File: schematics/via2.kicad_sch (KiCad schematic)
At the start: 12 parts, among them J11 Port A, J12 Port B, J13 myBus, Q2 2SB817, U10 W65C22, U11 74HC238

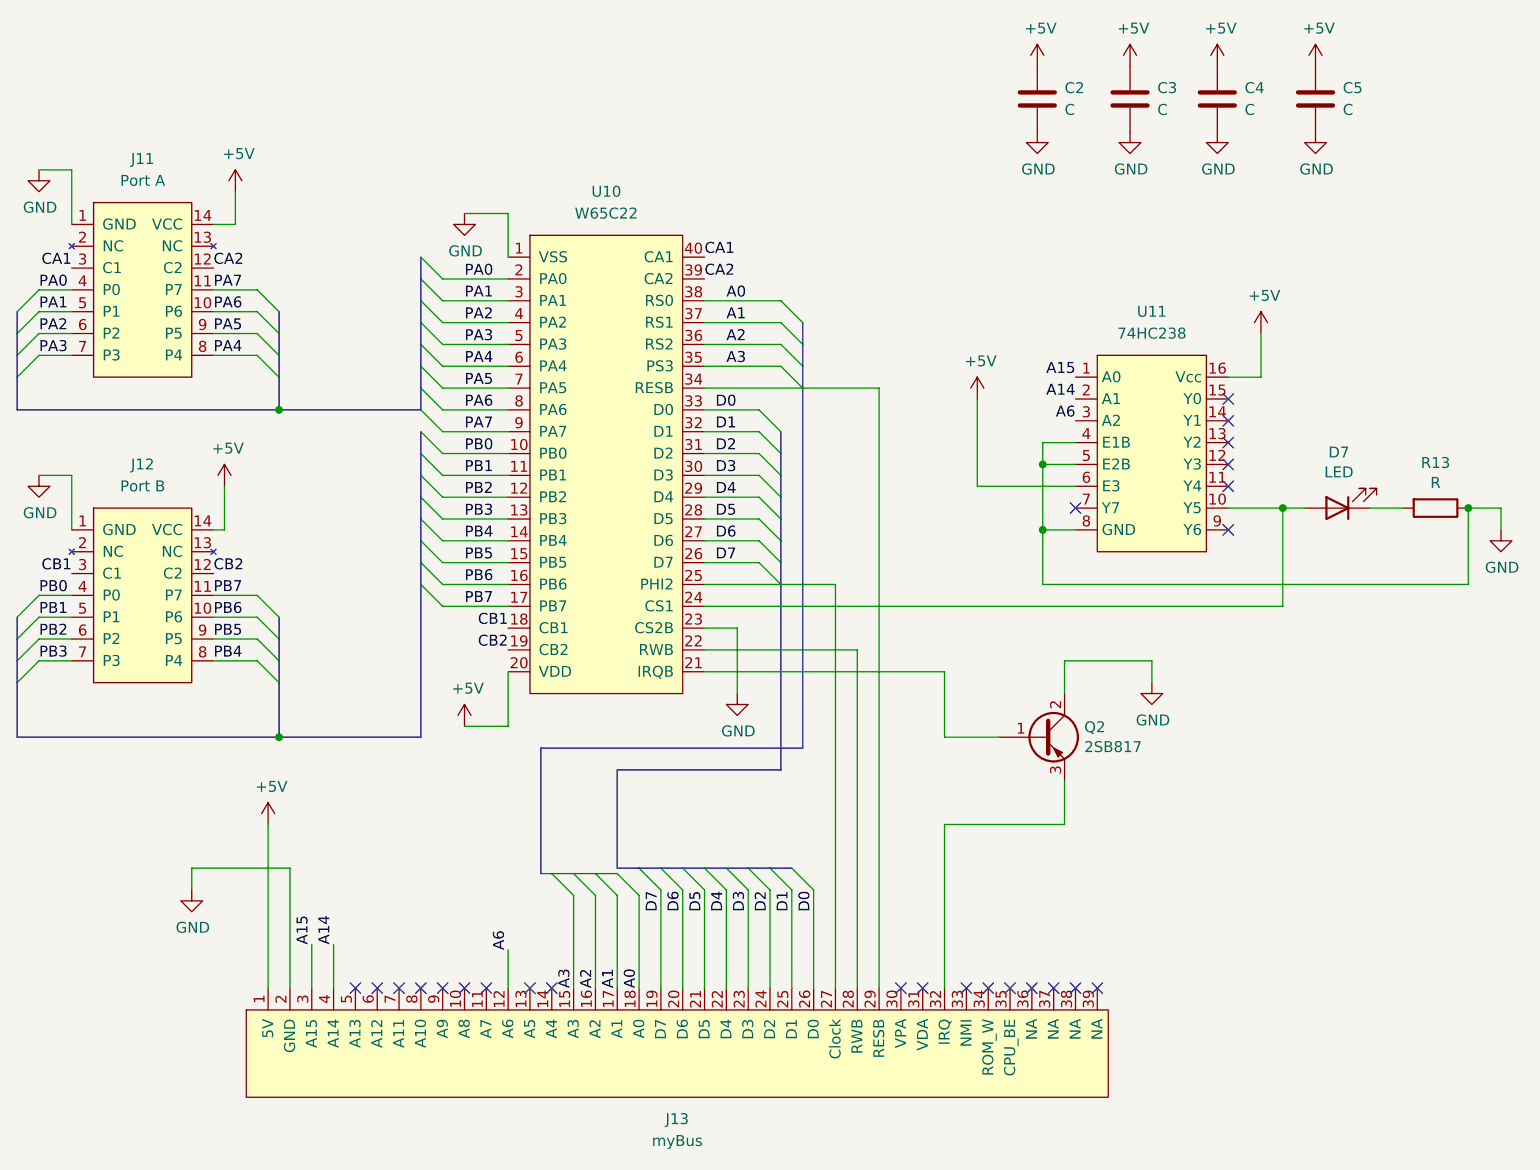
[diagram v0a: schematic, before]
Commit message: Fix errors in schematics
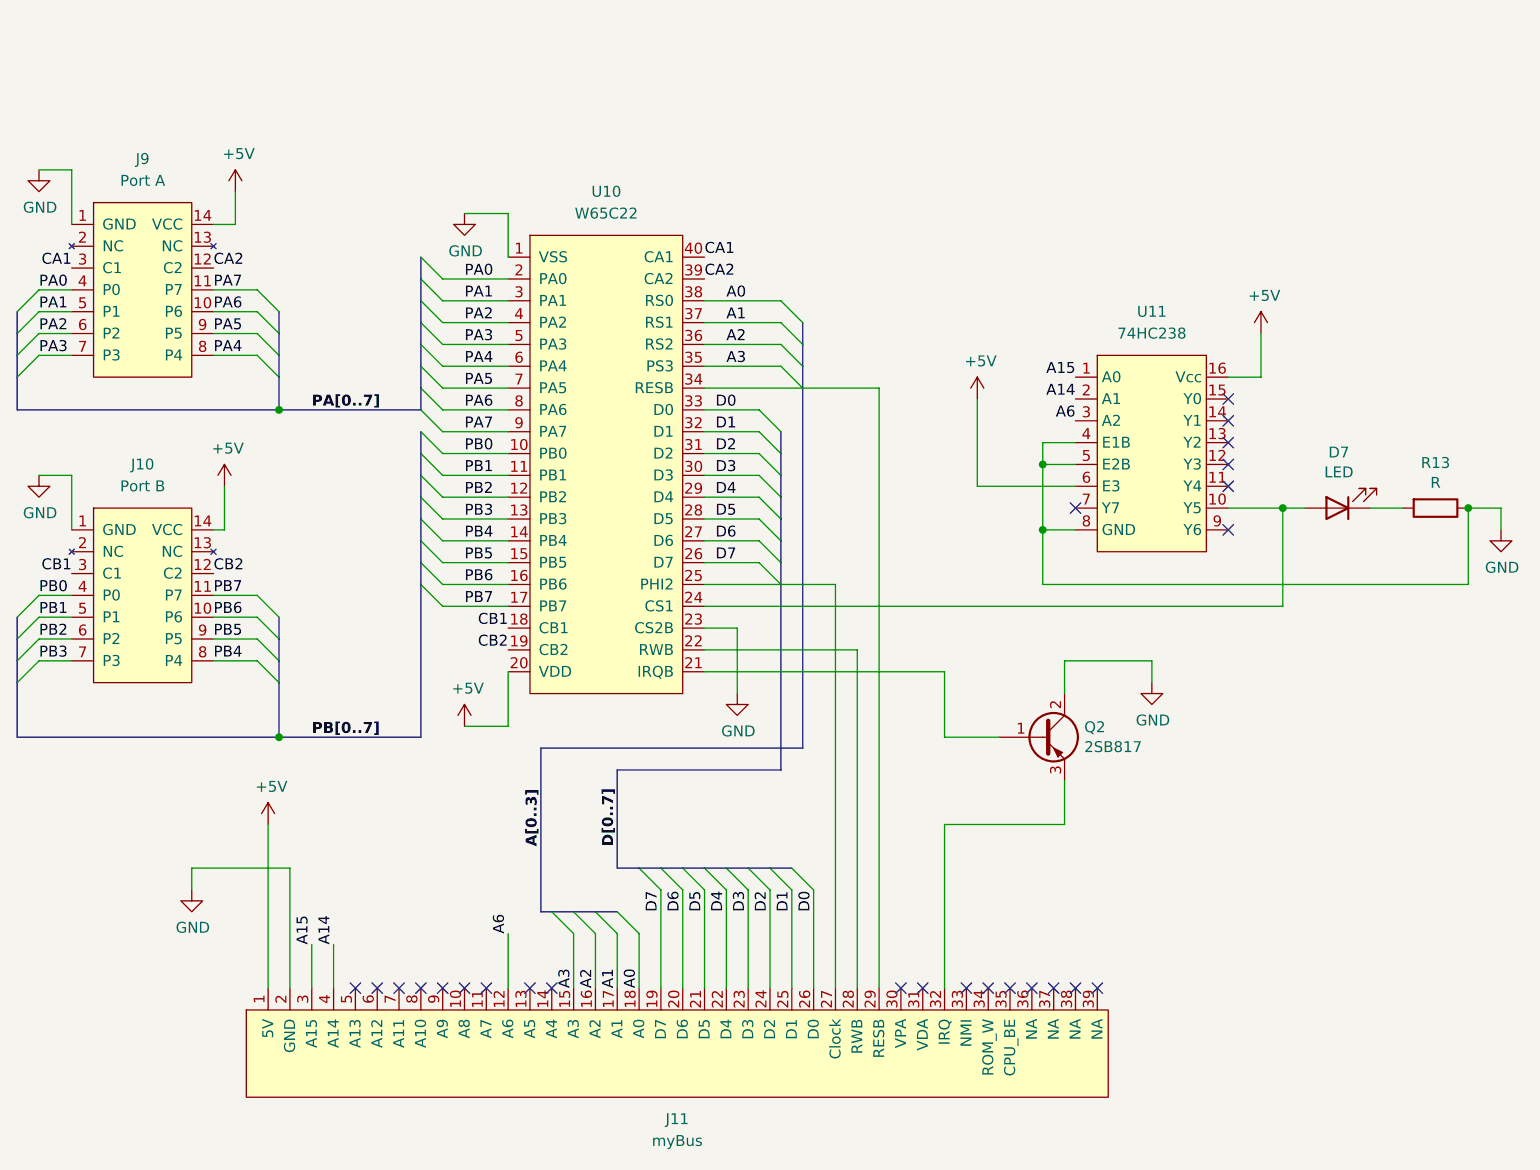
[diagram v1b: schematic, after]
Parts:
- removed C2, C3, C4, C5: C, Capacitor_THT:C_Disc_D4.3mm_W1.9mm_P5.00mm, symbol Device:C
- renumbered J12 to J10, J13 to J11, J11 to J9

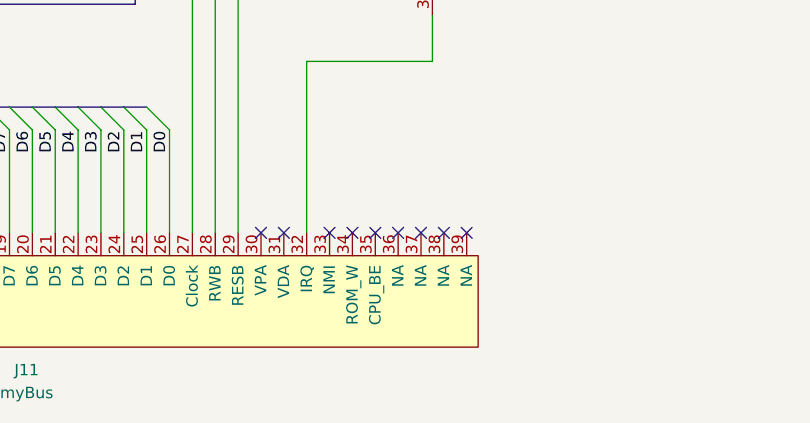
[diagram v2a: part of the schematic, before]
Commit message: Update ROM design
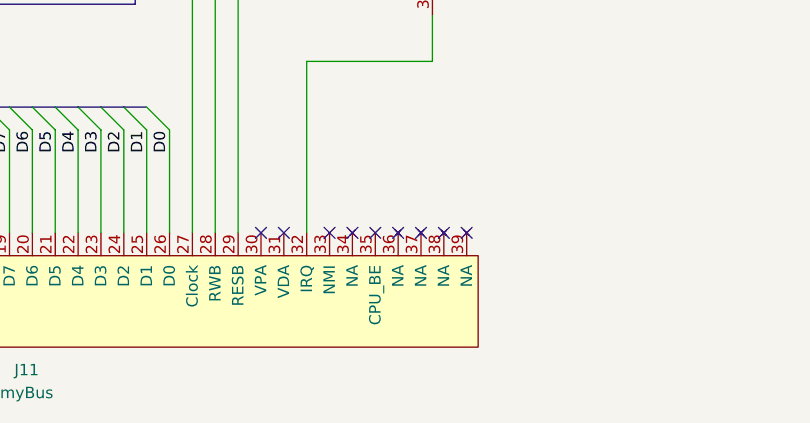
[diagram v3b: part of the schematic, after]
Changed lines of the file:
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@@
 	(label "D6"
 		(at 125.73 88.9 0)
-		(fields_autoplaced yes)
 		(effects
 			(font
@@
 	(label "PA4"
 		(at 96.52 68.58 0)
-		(fields_autoplaced yes)
 		(effects
 			(font
@@
 	(label "PB4"
 		(at 96.52 88.9 0)
-		(fields_autoplaced yes)
 		(effects
 			(font
@@
 	(label "PB[0..7]"
 		(at 78.74 111.76 0)
-		(fields_autoplaced yes)
 		(effects
 			(font
@@
 	(label "D4"
 		(at 127 132.08 90)
-		(fields_autoplaced yes)
 		(effects
 			(font
@@
 	(label "A3"
 		(at 127 68.58 0)
-		(fields_autoplaced yes)
 		(effects
 			(font
@@
 	(label "PB3"
 		(at 46.99 102.87 0)
-		(fields_autoplaced yes)
 		(effects
 			(font
@@
 	(label "A0"
 		(at 127 60.96 0)
-		(fields_autoplaced yes)
 		(effects
 			(font
@@
 	(label "A15"
 		(at 167.64 69.85 180)
-		(fields_autoplaced yes)
 		(effects
 			(font
@@
 	(label "PB0"
 		(at 96.52 78.74 0)
-		(fields_autoplaced yes)
 		(effects
 			(font
@@
 	(label "CA2"
 		(at 67.31 57.15 0)
-		(fields_autoplaced yes)
 		(effects
 			(font
@@
 	(label "A14"
 		(at 81.28 135.89 90)
-		(fields_autoplaced yes)
 		(effects
 			(font
@@
 	(label "A3"
 		(at 109.22 140.97 90)
-		(fields_autoplaced yes)
 		(effects
 			(font
@@
 	(label "A6"
 		(at 167.64 74.93 180)
-		(fields_autoplaced yes)
 		(effects
 			(font
@@
 	(label "CB2"
 		(at 101.6 101.6 180)
-		(fields_autoplaced yes)
 		(effects
 			(font
@@
 	(label "D4"
 		(at 125.73 83.82 0)
-		(fields_autoplaced yes)
 		(effects
 			(font
@@
 	(label "PB6"
 		(at 96.52 93.98 0)
-		(fields_autoplaced yes)
 		(effects
 			(font
@@
 	(label "A6"
 		(at 101.6 134.62 90)
-		(fields_autoplaced yes)
 		(effects
 			(font
@@
 	(label "PA5"
 		(at 67.31 64.77 0)
-		(fields_autoplaced yes)
 		(effects
 			(font
@@
 	(label "PB6"
 		(at 67.31 97.79 0)
-		(fields_autoplaced yes)
 		(effects
 			(font
@@
 	(label "PA7"
 		(at 67.31 59.69 0)
-		(fields_autoplaced yes)
 		(effects
 			(font
@@
 	(label "PB3"
 		(at 96.52 86.36 0)
-		(fields_autoplaced yes)
 		(effects
 			(font
@@
 	(label "A2"
 		(at 127 66.04 0)
-		(fields_autoplaced yes)
 		(effects
 			(font
@@
 	(label "CB2"
 		(at 67.31 92.71 0)
-		(fields_autoplaced yes)
 		(effects
 			(font
@@
 	(label "PB1"
 		(at 46.99 97.79 0)
-		(fields_autoplaced yes)
 		(effects
 			(font
@@
 	(label "PA6"
 		(at 96.52 73.66 0)
-		(fields_autoplaced yes)
 		(effects
 			(font
@@
 	(label "D6"
 		(at 121.92 132.08 90)
-		(fields_autoplaced yes)
 		(effects
 			(font
@@
 	(label "CB1"
 		(at 50.8 92.71 180)
-		(fields_autoplaced yes)
 		(effects
 			(font
@@
 	(label "D2"
 		(at 125.73 78.74 0)
-		(fields_autoplaced yes)
 		(effects
 			(font
@@
 	(label "D7"
 		(at 119.38 132.08 90)
-		(fields_autoplaced yes)
 		(effects
 			(font
@@
 	(label "A14"
 		(at 167.64 72.39 180)
-		(fields_autoplaced yes)
 		(effects
 			(font
@@
 	(label "PA5"
 		(at 96.52 71.12 0)
-		(fields_autoplaced yes)
 		(effects
 			(font
@@
 	(label "D3"
 		(at 125.73 81.28 0)
-		(fields_autoplaced yes)
 		(effects
 			(font
@@
 	(label "D0"
 		(at 125.73 73.66 0)
-		(fields_autoplaced yes)
 		(effects
 			(font
@@
 	(label "PA7"
 		(at 96.52 76.2 0)
-		(fields_autoplaced yes)
 		(effects
 			(font
@@
 	(label "D[0..7]"
 		(at 114.3 124.46 90)
-		(fields_autoplaced yes)
 		(effects
 			(font
@@
 	(label "D5"
 		(at 124.46 132.08 90)
-		(fields_autoplaced yes)
 		(effects
 			(font
@@
 	(label "A1"
 		(at 127 63.5 0)
-		(fields_autoplaced yes)
 		(effects
 			(font
@@
 	(label "PB5"
 		(at 96.52 91.44 0)
-		(fields_autoplaced yes)
 		(effects
 			(font
@@
 	(label "CA1"
 		(at 124.46 55.88 0)
-		(fields_autoplaced yes)
 		(effects
 			(font
@@
 	(label "A1"
 		(at 114.3 140.97 90)
-		(fields_autoplaced yes)
 		(effects
 			(font
@@
 	(label "PB1"
 		(at 96.52 81.28 0)
-		(fields_autoplaced yes)
 		(effects
 			(font
@@
 	(label "D0"
 		(at 137.16 132.08 90)
-		(fields_autoplaced yes)
 		(effects
 			(font
@@
 	(label "PB2"
 		(at 96.52 83.82 0)
-		(fields_autoplaced yes)
 		(effects
 			(font
@@
 	(label "PB7"
 		(at 96.52 96.52 0)
-		(fields_autoplaced yes)
 		(effects
 			(font
@@
 	(label "PA2"
 		(at 96.52 63.5 0)
-		(fields_autoplaced yes)
 		(effects
 			(font
@@
 	(label "PA3"
 		(at 46.99 67.31 0)
-		(fields_autoplaced yes)
 		(effects
 			(font
@@
 	(label "PA0"
 		(at 96.52 58.42 0)
-		(fields_autoplaced yes)
 		(effects
 			(font
@@
 	(label "D3"
 		(at 129.54 132.08 90)
-		(fields_autoplaced yes)
 		(effects
 			(font
@@
 	(label "A15"
 		(at 78.74 135.89 90)
-		(fields_autoplaced yes)
 		(effects
 			(font
@@
 	(label "PA6"
 		(at 67.31 62.23 0)
-		(fields_autoplaced yes)
 		(effects
 			(font
@@
 	(label "CA2"
 		(at 124.46 58.42 0)
-		(fields_autoplaced yes)
 		(effects
 			(font
@@
 	(label "D7"
 		(at 125.73 91.44 0)
-		(fields_autoplaced yes)
 		(effects
 			(font
@@
 	(label "D1"
 		(at 134.62 132.08 90)
-		(fields_autoplaced yes)
 		(effects
 			(font
@@
 	(label "PA4"
 		(at 67.31 67.31 0)
-		(fields_autoplaced yes)
 		(effects
 			(font
@@
 	(label "PB0"
 		(at 46.99 95.25 0)
-		(fields_autoplaced yes)
 		(effects
 			(font
@@
 	(label "PA1"
 		(at 96.52 60.96 0)
-		(fields_autoplaced yes)
 		(effects
 			(font
@@
 	(label "PB5"
 		(at 67.31 100.33 0)
-		(fields_autoplaced yes)
 		(effects
 			(font
@@
 	(label "A0"
 		(at 116.84 140.97 90)
-		(fields_autoplaced yes)
 		(effects
 			(font
@@
 	(label "PA1"
 		(at 46.99 62.23 0)
-		(fields_autoplaced yes)
 		(effects
 			(font
@@
 	(label "D1"
 		(at 125.73 76.2 0)
-		(fields_autoplaced yes)
 		(effects
 			(font
@@
 	(label "D2"
 		(at 132.08 132.08 90)
-		(fields_autoplaced yes)
 		(effects
 			(font
@@
 	(label "PB4"
 		(at 67.31 102.87 0)
-		(fields_autoplaced yes)
 		(effects
 			(font
@@
 	(label "D5"
 		(at 125.73 86.36 0)
-		(fields_autoplaced yes)
 		(effects
 			(font
@@
 	(label "A2"
 		(at 111.76 140.97 90)
-		(fields_autoplaced yes)
 		(effects
 			(font
@@
 	(label "PA0"
 		(at 46.99 59.69 0)
-		(fields_autoplaced yes)
 		(effects
 			(font
@@
 	(label "A[0..3]"
 		(at 105.41 124.46 90)
-		(fields_autoplaced yes)
 		(effects
 			(font
@@
 	(label "PA[0..7]"
 		(at 78.74 73.66 0)
-		(fields_autoplaced yes)
 		(effects
 			(font
@@
 	(label "CA1"
 		(at 50.8 57.15 180)
-		(fields_autoplaced yes)
 		(effects
 			(font
@@
 	(label "CB1"
 		(at 101.6 99.06 180)
-		(fields_autoplaced yes)
 		(effects
 			(font
@@
 	(label "PA3"
 		(at 96.52 66.04 0)
-		(fields_autoplaced yes)
 		(effects
 			(font
@@
 	(label "PB7"
 		(at 67.31 95.25 0)
-		(fields_autoplaced yes)
 		(effects
 			(font
@@
 	(label "PB2"
 		(at 46.99 100.33 0)
-		(fields_autoplaced yes)
 		(effects
 			(font
@@
 	(label "PA2"
 		(at 46.99 64.77 0)
-		(fields_autoplaced yes)
-		(effects
-			(font
+		(effects
+			(font
